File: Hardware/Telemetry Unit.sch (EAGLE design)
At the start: 52 parts, among them IC1 MEGA128-A, IC2 FT232RL, J2 503182-1852, J3 10118193-0001LF, Q1 10MHz, U1 MPL3115A2, U2 AOZ1280, U3 LSM6DS3

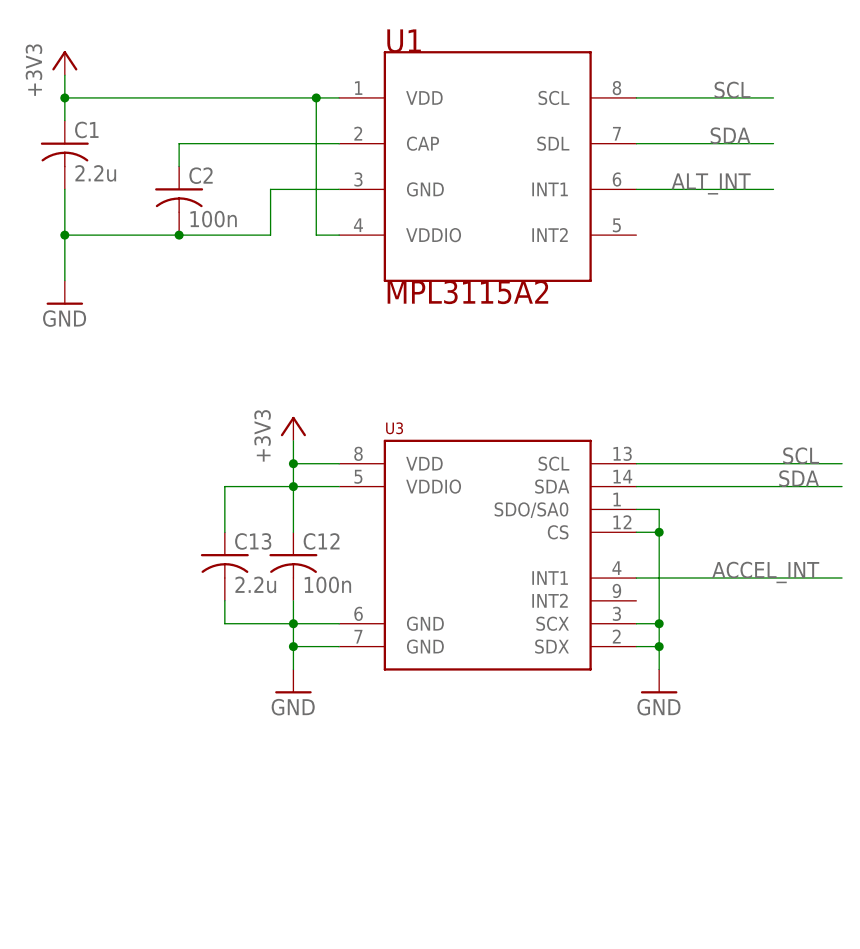
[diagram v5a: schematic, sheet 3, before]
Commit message: Wide-Range Accelerometer
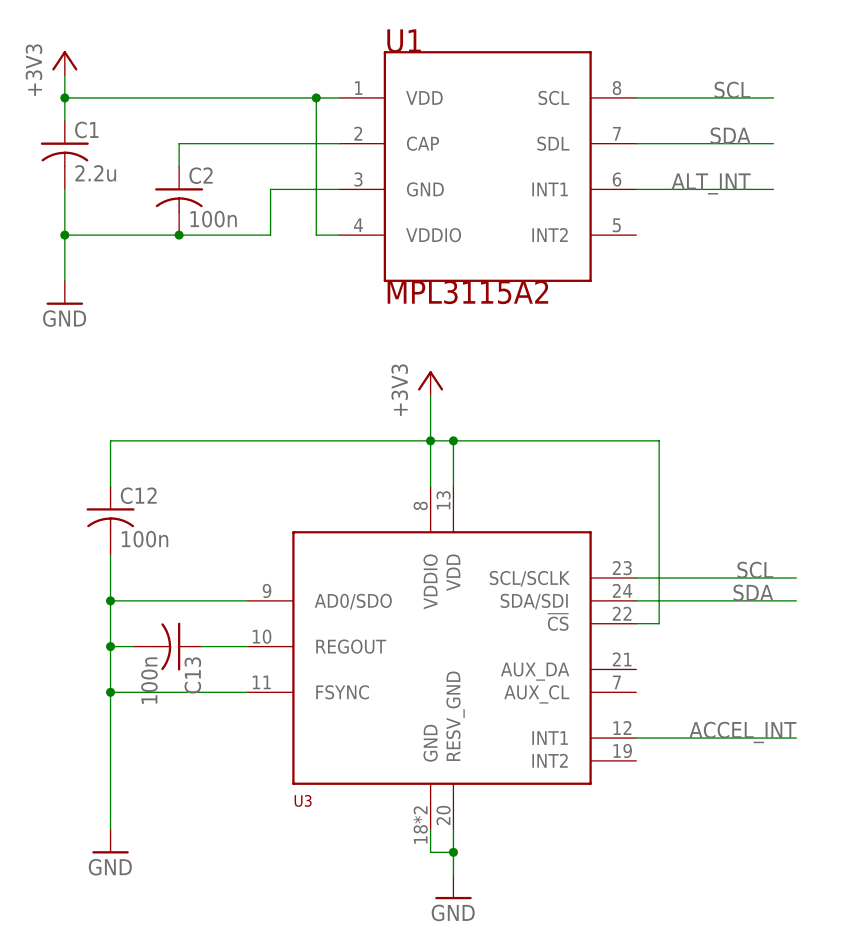
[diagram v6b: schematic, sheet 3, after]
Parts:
- C13: value 2.2u -> 100n
- U3: value LSM6DS3 -> ICM-20649; device TrackerPeripherals:LSM6DS3 -> TrackerPeripherals:ICM-20649
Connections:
- new net N$8: C13.1, U3.REGOUT
- net +3V3: now also U3.!CS; no longer C13.1
- net GND: now also U3.AD0/SDO, U3.FSYNC, U3.GND, U3.RESV_GND; no longer U3.CS, U3.GND@1, U3.GND@2, U3.SCX, U3.SDO/SA0, U3.SDX
- net SCL: now also U3.SCL/SCLK; no longer U3.SCL
- net SDA: now also U3.SDA/SDI; no longer U3.SDA
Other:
- moved on the sheet: C12, C13

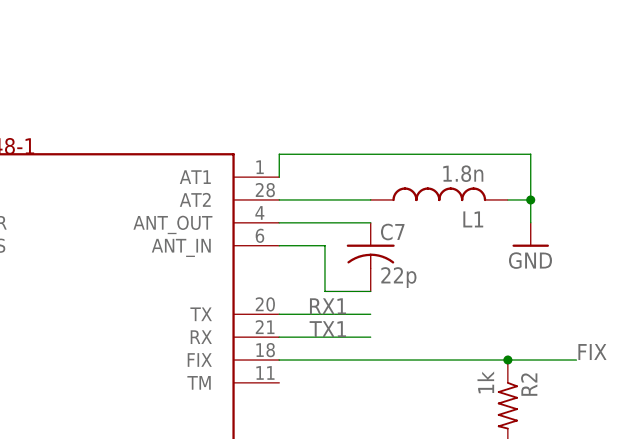
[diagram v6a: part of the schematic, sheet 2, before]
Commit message: 0 Ohm Tuning Resistor
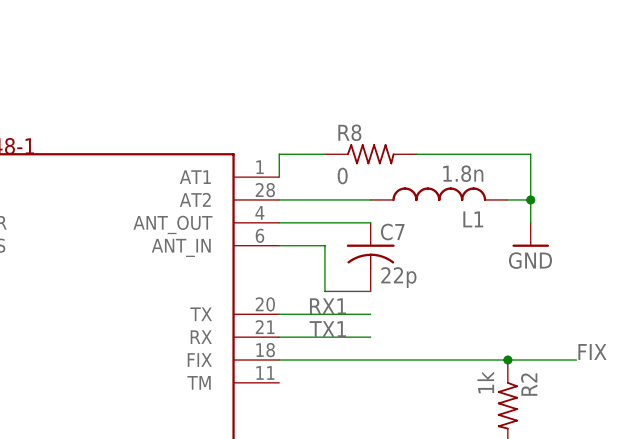
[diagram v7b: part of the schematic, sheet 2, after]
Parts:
- added R8: 0, resistor:R-US_R0603
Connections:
- new net N$21: GPS1.AT1, R8.1
- net GND: now also R8.2; no longer GPS1.AT1
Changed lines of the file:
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@@
 <part name="C12" library="resistor" library_urn="urn:adsk.eagle:library:348" deviceset="C-US" device="C0603" package3d_urn="urn:adsk.eagle:package:23616/2" value="100n"/>
 <part name="C13" library="resistor" library_urn="urn:adsk.eagle:library:348" deviceset="C-US" device="C0603" package3d_urn="urn:adsk.eagle:package:23616/2" value="100n"/>
+<part name="R8" library="resistor" library_urn="urn:adsk.eagle:library:348" deviceset="R-US_" device="R0603" package3d_urn="urn:adsk.eagle:package:23555/3" value="0"/>
 </parts>
 <sheets>
@@
 <instance part="GND9" gate="1" x="-20.32" y="45.72" smashed="yes">
 <attribute name="VALUE" x="-22.86" y="43.18" size="1.778" layer="96"/>
+</instance>
+<instance part="R8" gate="G$1" x="55.88" y="55.88" smashed="yes">
+<attribute name="NAME" x="52.07" y="57.3786" size="1.778" layer="95"/>
+<attribute name="VALUE" x="52.07" y="52.578" size="1.778" layer="96"/>
 </instance>
 </instances>
@@
 <pinref part="GND1" gate="1" pin="GND"/>
 <wire x1="73.66" y1="50.8" x2="73.66" y2="48.26" width="0.1524" layer="91"/>
-<pinref part="GPS1" gate="G$1" pin="AT1"/>
-<wire x1="45.72" y1="53.34" x2="45.72" y2="55.88" width="0.1524" layer="91"/>
-<wire x1="45.72" y1="55.88" x2="73.66" y2="55.88" width="0.1524" layer="91"/>
 <wire x1="73.66" y1="55.88" x2="73.66" y2="50.8" width="0.1524" layer="91"/>
 <junction x="73.66" y="50.8"/>
+<pinref part="R8" gate="G$1" pin="2"/>
+<wire x1="60.96" y1="55.88" x2="73.66" y2="55.88" width="0.1524" layer="91"/>
 </segment>
 <segment>
@@
 </segment>
 </net>
+<net name="N$21" class="0">
+<segment>
+<pinref part="GPS1" gate="G$1" pin="AT1"/>
+<wire x1="45.72" y1="53.34" x2="45.72" y2="55.88" width="0.1524" layer="91"/>
+<pinref part="R8" gate="G$1" pin="1"/>
+<wire x1="45.72" y1="55.88" x2="50.8" y2="55.88" width="0.1524" layer="91"/>
+</segment>
+</net>

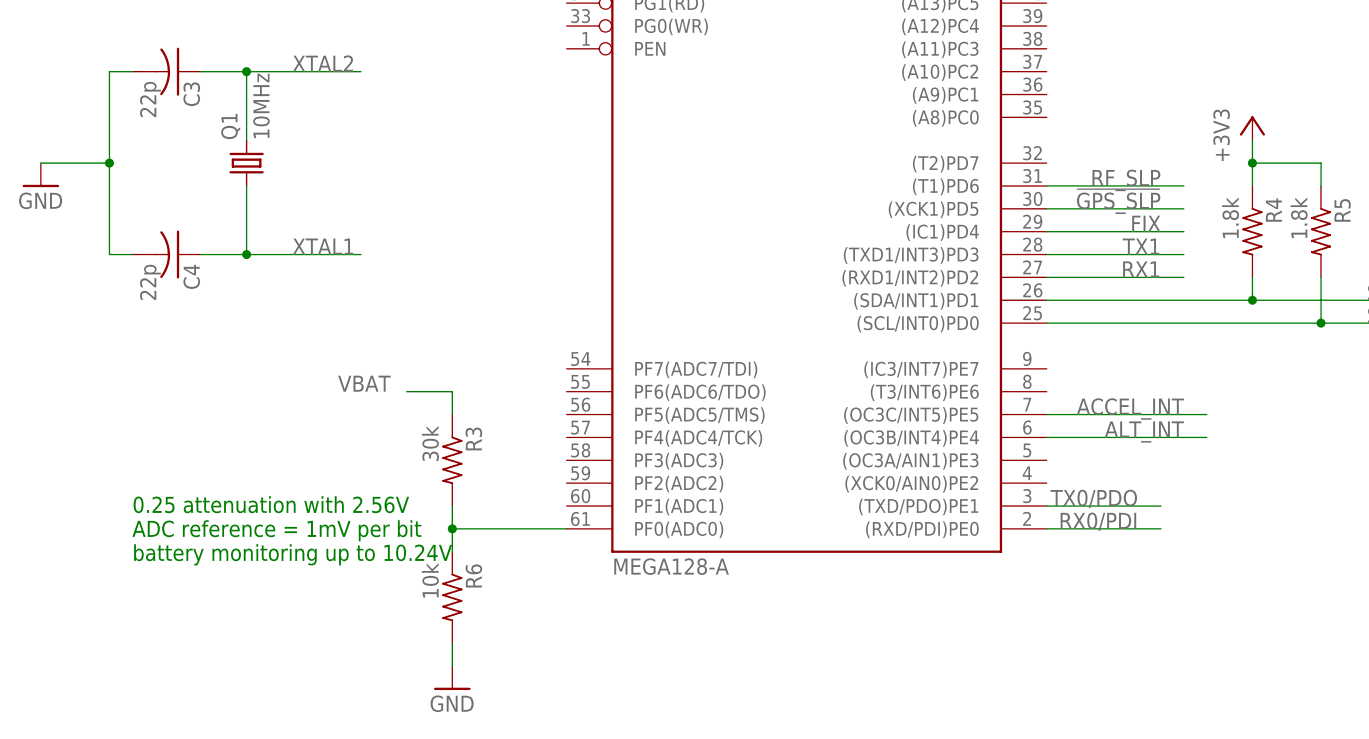
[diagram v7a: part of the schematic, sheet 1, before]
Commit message: Move GPS to long edge.  Much rerouting.  Shrunk board 0.25"
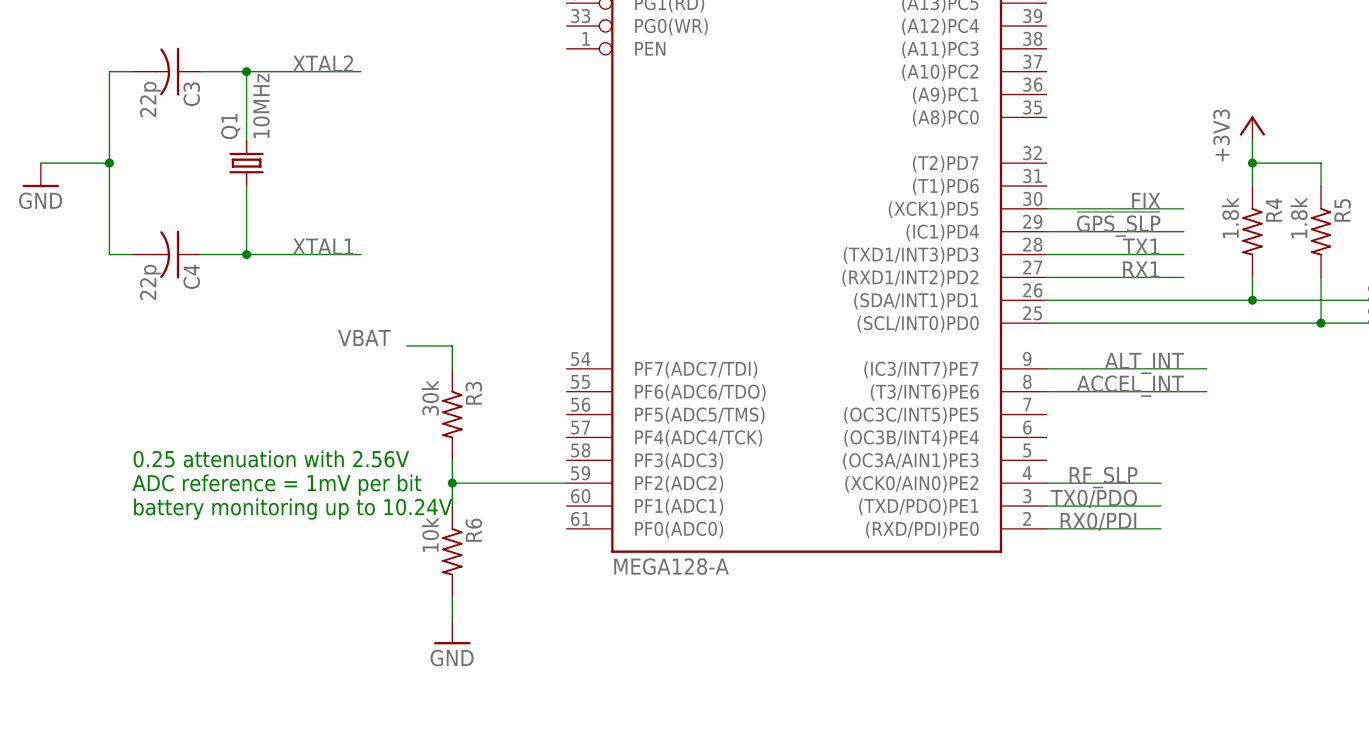
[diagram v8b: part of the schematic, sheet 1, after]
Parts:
- Q1: device crystal:CRYSTALHC49UP -> crystal-geyer_V1_0:KX-7
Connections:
- removed net N$22: F1.1, J3.VUSB
- new net 5V_USB: F1.1, IC2.VCC, J3.VUSB
- net !GPS_SLP: now also IC1.(IC1)PD4; no longer IC1.(XCK1)PD5
- net ACCEL_INT: now also IC1.(T3/INT6)PE6; no longer IC1.(OC3C/INT5)PE5
- net ALT_INT: now also IC1.(IC3/INT7)PE7; no longer IC1.(OC3B/INT4)PE4
- net FIX: now also IC1.(XCK1)PD5; no longer IC1.(IC1)PD4
- net N$5: now also IC1.PF2(ADC2); no longer IC1.PF0(ADC0)
- net RF_SLP: now also IC1.(XCK0/AIN0)PE2; no longer IC1.(T1)PD6
- net V_USB: no longer IC2.VCC
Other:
- moved on the sheet: J3, R3, R6
